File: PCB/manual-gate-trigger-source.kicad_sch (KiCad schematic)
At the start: 58 parts

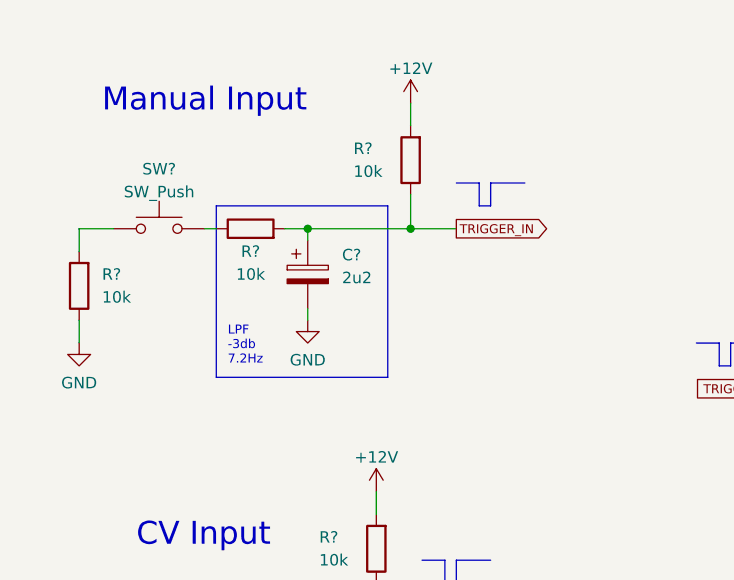
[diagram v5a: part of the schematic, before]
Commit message: :bug: Fix manual input circuit
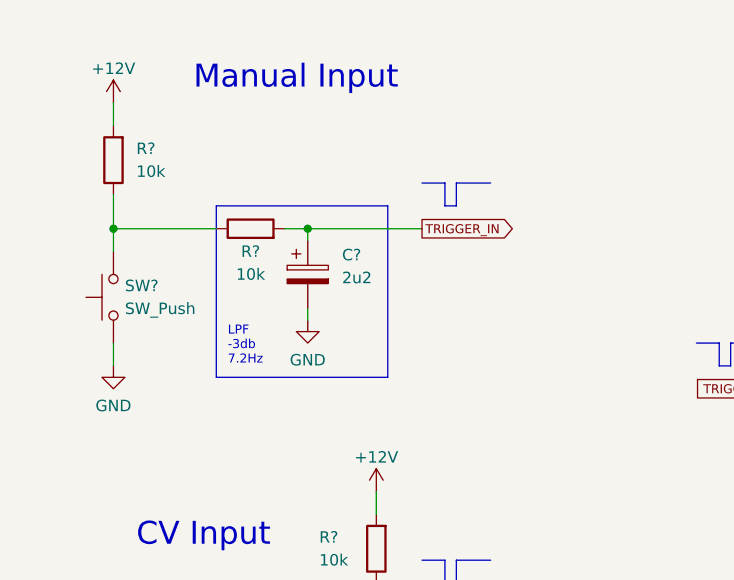
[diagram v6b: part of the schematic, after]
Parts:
- removed R?: 10k, symbol Device:R
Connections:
- net GND: now also SW?.1
- net TRIGGER_IN: no longer R?.1
- net at R?.1, SW?.2: now also R?.1
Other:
- moved on the sheet: R?, SW?
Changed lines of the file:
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@@
   (junction (at 198.12 138.43) (diameter 0) (color 0 0 0 0)
   )
+  (junction (at 24.13 40.64) (diameter 0) (color 0 0 0 0)
+  )
   (junction (at 104.14 44.45) (diameter 0) (color 0 0 0 0)
   )
@@
   )
   (junction (at 132.08 78.74) (diameter 0) (color 0 0 0 0)
-  )
-  (junction (at 57.15 40.64) (diameter 0) (color 0 0 0 0)
   )
   (junction (at 257.81 146.05) (diameter 0) (color 0 0 0 0)
@@
     (stroke (width 0) (type default) (color 0 0 0 0))
   )
-  (polyline (pts (xy 64.77 38.1) (xy 66.04 38.1))
+  (polyline (pts (xy 60.96 38.1) (xy 62.23 38.1))
     (stroke (width 0) (type solid) (color 0 0 0 0))
   )
@@
     (stroke (width 0) (type solid) (color 0 0 0 0))
   )
-  (wire (pts (xy 20.32 40.64) (xy 20.32 43.18))
-    (stroke (width 0) (type default) (color 0 0 0 0))
-  )
   (wire (pts (xy 262.89 46.99) (xy 266.7 46.99))
     (stroke (width 0) (type default) (color 0 0 0 0))
@@
     (stroke (width 0) (type default) (color 0 0 0 0))
   )
-  (wire (pts (xy 57.15 36.83) (xy 57.15 40.64))
-    (stroke (width 0) (type default) (color 0 0 0 0))
-  )
   (wire (pts (xy 104.14 78.74) (xy 132.08 78.74))
     (stroke (width 0) (type default) (color 0 0 0 0))
@@
     (stroke (width 0) (type default) (color 0 0 0 0))
   )
+  (wire (pts (xy 24.13 53.34) (xy 24.13 55.88))
+    (stroke (width 0) (type default) (color 0 0 0 0))
+  )
   (wire (pts (xy 194.31 44.45) (xy 194.31 48.26))
     (stroke (width 0) (type default) (color 0 0 0 0))
@@
     (stroke (width 0) (type default) (color 0 0 0 0))
   )
-  (polyline (pts (xy 66.04 38.1) (xy 66.04 35.56))
+  (polyline (pts (xy 62.23 38.1) (xy 62.23 35.56))
     (stroke (width 0) (type solid) (color 0 0 0 0))
   )
@@
     (stroke (width 0) (type default) (color 0 0 0 0))
   )
-  (wire (pts (xy 20.32 50.8) (xy 20.32 53.34))
+  (wire (pts (xy 24.13 36.83) (xy 24.13 40.64))
     (stroke (width 0) (type default) (color 0 0 0 0))
   )
@@
     (stroke (width 0) (type default) (color 0 0 0 0))
   )
-  (wire (pts (xy 57.15 26.67) (xy 57.15 29.21))
+  (wire (pts (xy 24.13 26.67) (xy 24.13 29.21))
     (stroke (width 0) (type default) (color 0 0 0 0))
   )
@@
     (stroke (width 0) (type default) (color 0 0 0 0))
   )
+  (wire (pts (xy 24.13 40.64) (xy 24.13 43.18))
+    (stroke (width 0) (type default) (color 0 0 0 0))
+  )
   (polyline (pts (xy 60.96 77.47) (xy 60.96 80.01))
     (stroke (width 0) (type solid) (color 0 0 0 0))
@@
     (stroke (width 0) (type default) (color 0 0 0 0))
   )
-  (polyline (pts (xy 64.77 35.56) (xy 64.77 38.1))
+  (polyline (pts (xy 60.96 35.56) (xy 60.96 38.1))
     (stroke (width 0) (type solid) (color 0 0 0 0))
   )
@@
     (stroke (width 0) (type default) (color 0 0 0 0))
   )
-  (wire (pts (xy 34.29 40.64) (xy 35.56 40.64))
-    (stroke (width 0) (type default) (color 0 0 0 0))
-  )
   (wire (pts (xy 265.43 49.53) (xy 265.43 59.69))
     (stroke (width 0) (type default) (color 0 0 0 0))
@@
     (stroke (width 0) (type default) (color 0 0 0 0))
   )
-  (wire (pts (xy 57.15 40.64) (xy 62.23 40.64))
+  (wire (pts (xy 45.72 40.64) (xy 58.42 40.64))
     (stroke (width 0) (type default) (color 0 0 0 0))
   )
@@
     (stroke (width 0) (type default) (color 0 0 0 0))
   )
-  (polyline (pts (xy 62.23 35.56) (xy 64.77 35.56))
+  (polyline (pts (xy 58.42 35.56) (xy 60.96 35.56))
     (stroke (width 0) (type solid) (color 0 0 0 0))
   )
@@
     (stroke (width 0) (type solid) (color 0 0 0 0))
   )
-  (wire (pts (xy 20.32 40.64) (xy 24.13 40.64))
+  (wire (pts (xy 24.13 40.64) (xy 35.56 40.64))
     (stroke (width 0) (type default) (color 0 0 0 0))
   )
@@
     (stroke (width 0) (type default) (color 0 0 0 0))
   )
-  (wire (pts (xy 45.72 40.64) (xy 57.15 40.64))
-    (stroke (width 0) (type default) (color 0 0 0 0))
-  )
   (wire (pts (xy 168.91 143.51) (xy 167.64 143.51))
     (stroke (width 0) (type default) (color 0 0 0 0))
@@
     (stroke (width 0) (type solid) (color 0 0 0 0))
   )
-  (polyline (pts (xy 66.04 35.56) (xy 69.85 35.56))
+  (polyline (pts (xy 62.23 35.56) (xy 66.04 35.56))
     (stroke (width 0) (type solid) (color 0 0 0 0))
   )
@@
     (effects (font (size 1 1)) (justify left bottom))
   )
-  (text "Manual Input" (at 22.86 27.94 0)
+  (text "Manual Input" (at 33.02 25.4 0)
     (effects (font (size 2.54 2.54)) (justify left bottom))
   )
@@
     )
   )
-  (global_label "TRIGGER_IN" (shape output) (at 62.23 40.64 0) (fields_autoplaced)
+  (global_label "TRIGGER_IN" (shape output) (at 58.42 40.64 0) (fields_autoplaced)
     (effects (font (size 1 1)) (justify left))
-    (property "Intersheet References" "${INTERSHEET_REFS}" (id 0) (at 72.5586 40.5775 0)
+    (property "Intersheet References" "${INTERSHEET_REFS}" (id 0) (at 68.7486 40.5775 0)
       (effects (font (size 1 1)) (justify left) hide)
     )
@@
     (pin "2")
   )
-  (symbol (lib_id "power:GND") (at 20.32 53.34 0) (unit 1)
-    (in_bom yes) (on_board yes) (fields_autoplaced)
-    (property "Reference" "#PWR?" (id 0) (at 20.32 59.69 0)
-      (effects (font (size 1.27 1.27)) hide)
-    )
-    (property "Value" "GND" (id 1) (at 20.32 57.7834 0))
-    (property "Footprint" "" (id 2) (at 20.32 53.34 0)
-      (effects (font (size 1.27 1.27)) hide)
-    )
-    (property "Datasheet" "" (id 3) (at 20.32 53.34 0)
+  (symbol (lib_id "power:GND") (at 24.13 55.88 0) (unit 1)
+    (in_bom yes) (on_board yes) (fields_autoplaced)
+    (property "Reference" "#PWR?" (id 0) (at 24.13 62.23 0)
+      (effects (font (size 1.27 1.27)) hide)
+    )
+    (property "Value" "GND" (id 1) (at 24.13 60.3234 0))
+    (property "Footprint" "" (id 2) (at 24.13 55.88 0)
+      (effects (font (size 1.27 1.27)) hide)
+    )
+    (property "Datasheet" "" (id 3) (at 24.13 55.88 0)
       (effects (font (size 1.27 1.27)) hide)
     )
@@
     (pin "2")
   )
-  (symbol (lib_id "Switch:SW_Push") (at 29.21 40.64 0) (unit 1)
-    (in_bom yes) (on_board yes) (fields_autoplaced)
-    (property "Reference" "SW?" (id 0) (at 29.21 34.0192 0))
-    (property "Value" "SW_Push" (id 1) (at 29.21 36.5561 0))
-    (property "Footprint" "Button_Switch_Keyboard:SW_Cherry_MX_1.00u_PCB" (id 2) (at 29.21 35.56 0)
-      (effects (font (size 1.27 1.27)) hide)
-    )
-    (property "Datasheet" "~" (id 3) (at 29.21 35.56 0)
+  (symbol (lib_id "Switch:SW_Push") (at 24.13 48.26 90) (unit 1)
+    (in_bom yes) (on_board yes) (fields_autoplaced)
+    (property "Reference" "SW?" (id 0) (at 25.4 46.9899 90)
+      (effects (font (size 1.27 1.27)) (justify right))
+    )
+    (property "Value" "SW_Push" (id 1) (at 25.4 49.5299 90)
+      (effects (font (size 1.27 1.27)) (justify right))
+    )
+    (property "Footprint" "Button_Switch_Keyboard:SW_Cherry_MX_1.00u_PCB" (id 2) (at 19.05 48.26 0)
+      (effects (font (size 1.27 1.27)) hide)
+    )
+    (property "Datasheet" "~" (id 3) (at 19.05 48.26 0)
       (effects (font (size 1.27 1.27)) hide)
     )
@@
     (pin "3")
   )
-  (symbol (lib_id "Device:R") (at 20.32 46.99 180) (unit 1)
-    (in_bom yes) (on_board yes)
-    (property "Reference" "R?" (id 0) (at 22.86 45.7199 0)
-      (effects (font (size 1.27 1.27)) (justify right))
-    )
-    (property "Value" "10k" (id 1) (at 22.86 48.26 0)
-      (effects (font (size 1.27 1.27)) (justify right))
-    )
-    (property "Footprint" "" (id 2) (at 22.098 46.99 90)
-      (effects (font (size 1.27 1.27)) hide)
-    )
-    (property "Datasheet" "~" (id 3) (at 20.32 46.99 0)
-      (effects (font (size 1.27 1.27)) hide)
-    )
-    (pin "1")
-    (pin "2")
-  )
   (symbol (lib_id "power:GND") (at 251.46 72.39 0) (unit 1)
     (in_bom yes) (on_board yes) (fields_autoplaced)
@@
     (pin "2")
   )
-  (symbol (lib_id "Device:R") (at 57.15 33.02 180) (unit 1)
-    (in_bom yes) (on_board yes)
-    (property "Reference" "R?" (id 0) (at 50.8 31.7499 0)
-      (effects (font (size 1.27 1.27)) (justify right))
-    )
-    (property "Value" "10k" (id 1) (at 50.8 34.29 0)
-      (effects (font (size 1.27 1.27)) (justify right))
-    )
-    (property "Footprint" "" (id 2) (at 58.928 33.02 90)
-      (effects (font (size 1.27 1.27)) hide)
-    )
-    (property "Datasheet" "~" (id 3) (at 57.15 33.02 0)
+  (symbol (lib_id "Device:R") (at 24.13 33.02 180) (unit 1)
+    (in_bom yes) (on_board yes)
+    (property "Reference" "R?" (id 0) (at 26.67 31.7499 0)
+      (effects (font (size 1.27 1.27)) (justify right))
+    )
+    (property "Value" "10k" (id 1) (at 26.67 34.29 0)
+      (effects (font (size 1.27 1.27)) (justify right))
+    )
+    (property "Footprint" "" (id 2) (at 25.908 33.02 90)
+      (effects (font (size 1.27 1.27)) hide)
+    )
+    (property "Datasheet" "~" (id 3) (at 24.13 33.02 0)
       (effects (font (size 1.27 1.27)) hide)
     )
@@
     (pin "1")
   )
-  (symbol (lib_id "power:+12V") (at 57.15 26.67 0) (unit 1)
-    (in_bom yes) (on_board yes)
-    (property "Reference" "#PWR?" (id 0) (at 57.15 30.48 0)
-      (effects (font (size 1.27 1.27)) hide)
-    )
-    (property "Value" "+12V" (id 1) (at 57.15 22.86 0))
-    (property "Footprint" "" (id 2) (at 57.15 26.67 0)
-      (effects (font (size 1.27 1.27)) hide)
-    )
-    (property "Datasheet" "" (id 3) (at 57.15 26.67 0)
+  (symbol (lib_id "power:+12V") (at 24.13 26.67 0) (unit 1)
+    (in_bom yes) (on_board yes)
+    (property "Reference" "#PWR?" (id 0) (at 24.13 30.48 0)
+      (effects (font (size 1.27 1.27)) hide)
+    )
+    (property "Value" "+12V" (id 1) (at 24.13 22.86 0))
+    (property "Footprint" "" (id 2) (at 24.13 26.67 0)
+      (effects (font (size 1.27 1.27)) hide)
+    )
+    (property "Datasheet" "" (id 3) (at 24.13 26.67 0)
       (effects (font (size 1.27 1.27)) hide)
     )
@@
       (reference "R?") (unit 1) (value "10k") (footprint "")
     )
-    (path "/d81949eb-251b-4c42-89be-c8ce27ab6d4a"
-      (reference "R?") (unit 1) (value "10k") (footprint "")
-    )

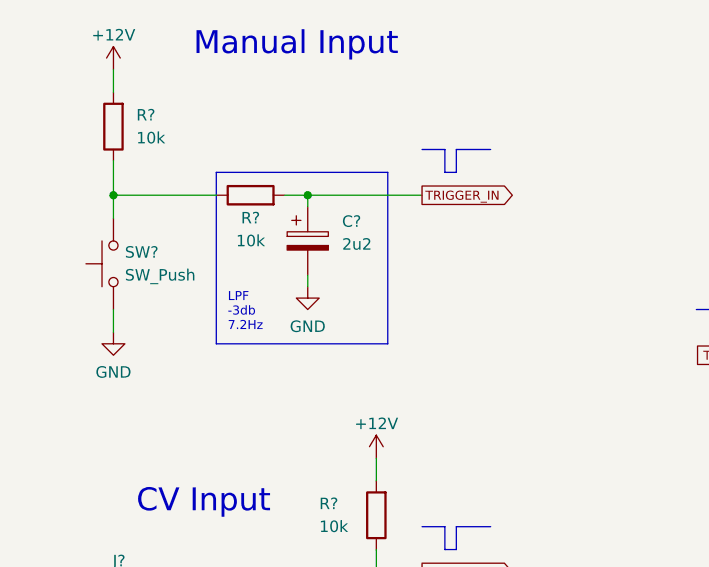
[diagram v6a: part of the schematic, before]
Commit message: :wrench: Adjust manual input LPF to match voltage selector
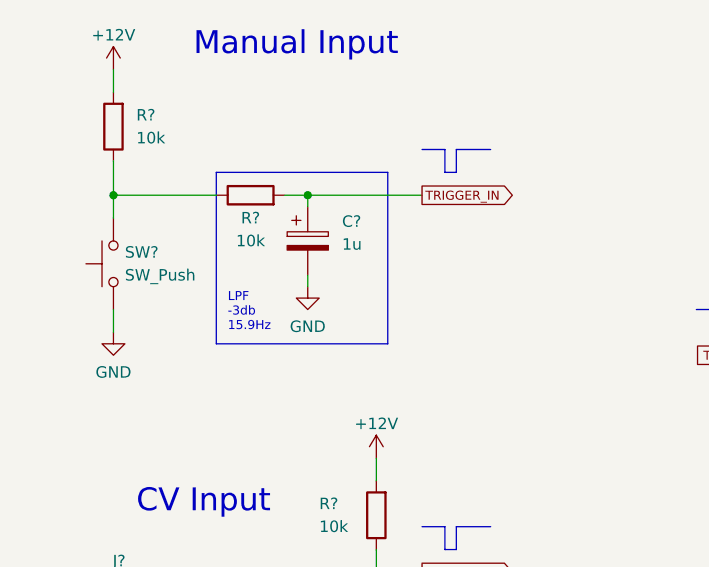
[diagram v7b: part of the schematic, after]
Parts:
- C?: value 2u2 -> 1u
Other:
- note removed: "LPF -3db 7.2Hz"
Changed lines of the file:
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@@
     (effects (font (size 2.54 2.54)) (justify left bottom))
+  )
+  (text "LPF\n-3db\n15.9Hz" (at 36.83 55.88 0)
+    (effects (font (size 1 1)) (justify left bottom))
   )
   (text "PWR Filter and Protection\n" (at 194.31 157.48 0)
@@
   )
   (text "HPF" (at 106.68 49.53 0)
-    (effects (font (size 1 1)) (justify left bottom))
-  )
-  (text "LPF\n-3db\n7.2Hz" (at 36.83 55.88 0)
     (effects (font (size 1 1)) (justify left bottom))
   )
@@
       (effects (font (size 1.27 1.27)) (justify left))
     )
-    (property "Value" "2u2" (id 1) (at 49.53 46.1009 0)
+    (property "Value" "1u" (id 1) (at 49.53 46.1009 0)
       (effects (font (size 1.27 1.27)) (justify left))
     )
@@
     )
     (path "/c910e764-5d8b-4c6f-8f0a-d8089475c0e6"
-      (reference "C?") (unit 1) (value "2u2") (footprint "")
+      (reference "C?") (unit 1) (value "1u") (footprint "")
     )
     (path "/d21e2ec8-6a0c-45ba-a5a2-590471f5aac9"

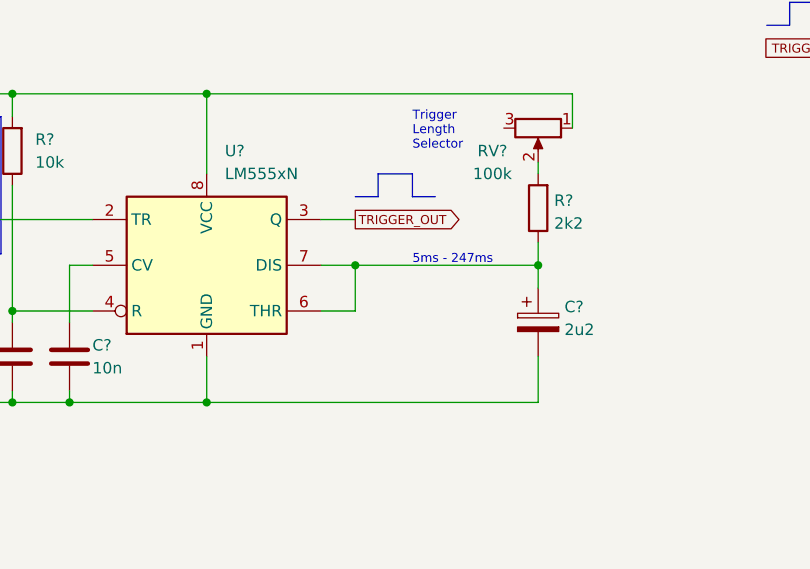
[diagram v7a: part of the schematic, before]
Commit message: :art: Tune RC values for trigger-length selector
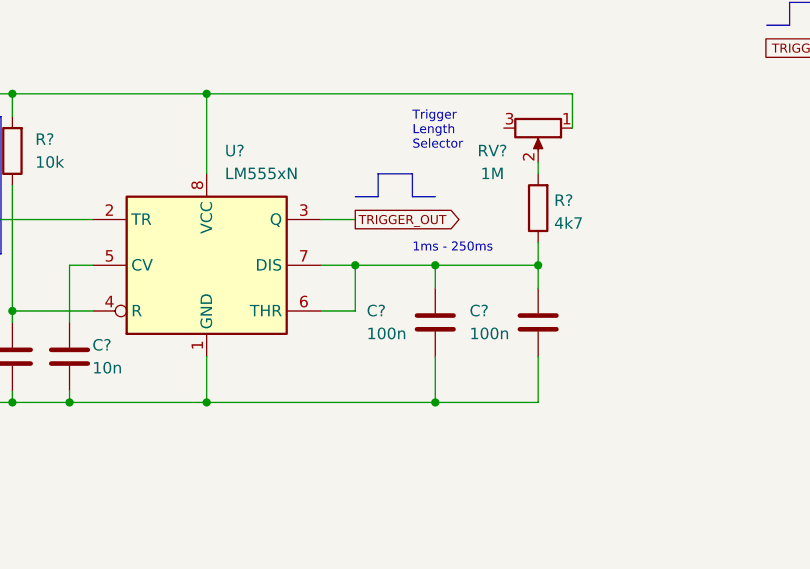
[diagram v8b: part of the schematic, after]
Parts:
- removed C?: 2u2, symbol Device:C_Polarized
- added C? (x2): 100n, symbol Device:C
- R?: value 2k2 -> 4k7
- RV?: value 100k -> 1M
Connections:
- net GND: now also C?.2, C?.2
- net at R?.1, U?.6 (THR), U?.7 (DIS): now also C?.1, C?.1
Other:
- note added: "1ms - 250ms"
- note removed: "5ms - 247ms"
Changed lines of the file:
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@@
   (junction (at 132.08 44.45) (diameter 0) (color 0 0 0 0)
   )
+  (junction (at 179.07 78.74) (diameter 0) (color 0 0 0 0)
+  )
   (junction (at 124.46 58.42) (diameter 0) (color 0 0 0 0)
   )
@@
   )
   (junction (at 132.08 78.74) (diameter 0) (color 0 0 0 0)
+  )
+  (junction (at 179.07 63.5) (diameter 0) (color 0 0 0 0)
   )
   (junction (at 257.81 146.05) (diameter 0) (color 0 0 0 0)
@@
     (stroke (width 0) (type default) (color 0 0 0 0))
   )
-  (wire (pts (xy 153.67 78.74) (xy 190.5 78.74))
+  (wire (pts (xy 153.67 78.74) (xy 179.07 78.74))
     (stroke (width 0) (type default) (color 0 0 0 0))
   )
@@
     (stroke (width 0) (type default) (color 0 0 0 0))
   )
+  (wire (pts (xy 179.07 78.74) (xy 190.5 78.74))
+    (stroke (width 0) (type default) (color 0 0 0 0))
+  )
   (wire (pts (xy 229.87 39.37) (xy 231.14 39.37))
     (stroke (width 0) (type default) (color 0 0 0 0))
@@
     (stroke (width 0) (type default) (color 0 0 0 0))
   )
+  (wire (pts (xy 179.07 73.66) (xy 179.07 78.74))
+    (stroke (width 0) (type default) (color 0 0 0 0))
+  )
   (wire (pts (xy 257.81 138.43) (xy 273.05 138.43))
     (stroke (width 0) (type default) (color 0 0 0 0))
@@
     (stroke (width 0) (type default) (color 0 0 0 0))
   )
+  (wire (pts (xy 179.07 63.5) (xy 190.5 63.5))
+    (stroke (width 0) (type default) (color 0 0 0 0))
+  )
   (wire (pts (xy 232.41 138.43) (xy 257.81 138.43))
     (stroke (width 0) (type default) (color 0 0 0 0))
@@
     (stroke (width 0) (type default) (color 0 0 0 0))
   )
+  (wire (pts (xy 179.07 63.5) (xy 179.07 66.04))
+    (stroke (width 0) (type default) (color 0 0 0 0))
+  )
   (wire (pts (xy 243.84 39.37) (xy 242.57 39.37))
     (stroke (width 0) (type default) (color 0 0 0 0))
@@
     (stroke (width 0) (type default) (color 0 0 0 0))
   )
-  (wire (pts (xy 170.18 63.5) (xy 190.5 63.5))
+  (wire (pts (xy 170.18 63.5) (xy 179.07 63.5))
     (stroke (width 0) (type default) (color 0 0 0 0))
   )
@@
     (effects (font (size 1.27 1.27)) (justify left bottom))
   )
-  (text "5ms - 247ms" (at 176.53 63.5 0)
+  (text "1ms - 250ms" (at 176.53 62.23 0)
     (effects (font (size 1 1)) (justify left bottom))
   )
@@
     (pin "2")
   )
-  (symbol (lib_id "Device:C_Polarized") (at 190.5 69.85 0) (unit 1)
-    (in_bom yes) (on_board yes) (fields_autoplaced)
-    (property "Reference" "C?" (id 0) (at 193.421 68.1263 0)
-      (effects (font (size 1.27 1.27)) (justify left))
-    )
-    (property "Value" "2u2" (id 1) (at 193.421 70.6632 0)
+  (symbol (lib_id "Device:C") (at 190.5 69.85 0) (unit 1)
+    (in_bom yes) (on_board yes)
+    (property "Reference" "C?" (id 0) (at 182.88 68.58 0)
+      (effects (font (size 1.27 1.27)) (justify left))
+    )
+    (property "Value" "100n" (id 1) (at 182.88 71.12 0)
       (effects (font (size 1.27 1.27)) (justify left))
     )
@@
     (pin "2")
   )
+  (symbol (lib_id "Device:C") (at 179.07 69.85 0) (unit 1)
+    (in_bom yes) (on_board yes)
+    (property "Reference" "C?" (id 0) (at 171.45 68.58 0)
+      (effects (font (size 1.27 1.27)) (justify left))
+    )
+    (property "Value" "100n" (id 1) (at 171.45 71.12 0)
+      (effects (font (size 1.27 1.27)) (justify left))
+    )
+    (property "Footprint" "" (id 2) (at 180.0352 73.66 0)
+      (effects (font (size 1.27 1.27)) hide)
+    )
+    (property "Datasheet" "~" (id 3) (at 179.07 69.85 0)
+      (effects (font (size 1.27 1.27)) hide)
+    )
+    (pin "1")
+    (pin "2")
+  )
   (symbol (lib_id "Device:R") (at 190.5 57.15 180) (unit 1)
     (in_bom yes) (on_board yes) (fields_autoplaced)
@@
       (effects (font (size 1.27 1.27)) (justify right))
     )
-    (property "Value" "2k2" (id 1) (at 192.278 58.8522 0)
+    (property "Value" "4k7" (id 1) (at 192.278 58.8522 0)
       (effects (font (size 1.27 1.27)) (justify right))
     )
@@
     (in_bom yes) (on_board yes)
     (property "Reference" "RV?" (id 0) (at 185.42 50.8 90))
-    (property "Value" "100k" (id 1) (at 185.42 53.34 90))
+    (property "Value" "1M" (id 1) (at 185.42 53.34 90))
     (property "Footprint" "" (id 2) (at 190.5 48.26 0)
       (effects (font (size 1.27 1.27)) hide)
@@
       (reference "C?") (unit 1) (value "10n") (footprint "")
     )
-    (path "/90788551-bdc4-4dcd-9cb8-fffcee0cf080"
-      (reference "C?") (unit 1) (value "2u2") (footprint "")
+    (path "/902fa357-c973-4d84-b1e4-cafe76121223"
+      (reference "C?") (unit 1) (value "100n") (footprint "")
     )
     (path "/9106c957-e8c5-46cd-8a2b-6a06cdafbfb6"
       (reference "C?") (unit 1) (value "10u") (footprint "")
     )
+    (path "/93343392-a67d-45ff-a4e8-e429cd9542fc"
+      (reference "C?") (unit 1) (value "100n") (footprint "")
+    )
     (path "/ae769598-1210-436a-b10d-6ce42e800bcb"
       (reference "C?") (unit 1) (value "100n") (footprint "")
@@
     )
     (path "/9b1418bd-cfcd-4c7b-a3f1-f1dc5c5b0f85"
-      (reference "R?") (unit 1) (value "2k2") (footprint "")
+      (reference "R?") (unit 1) (value "4k7") (footprint "")
     )
     (path "/bcb7582a-d44e-40a1-9466-31e89777ed69"
@@
     )
     (path "/d1dab4c4-3e17-4009-b908-f3f0b3370c6f"
-      (reference "RV?") (unit 1) (value "100k") (footprint "")
+      (reference "RV?") (unit 1) (value "1M") (footprint "")
     )
     (path "/7a5a16b9-da66-42bb-a529-0b67e4242f75"
